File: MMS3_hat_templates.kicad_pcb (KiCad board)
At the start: 4 copper layers, 100 x 50 mm, 55 parts, among them J1 Chainbus in, J2 Chainbus Out, J3 Conn_01x04_Pin, J4 AMASS XT60 Male, J5 AMASS XT60 Female, J8 Conn_01x03_Pin, SW1 SW_DIP_x04, U1 SN74CB3Q3384APW, U2 M24C64, U4 AMS1117, U5 LM2596HVS-ADJRG

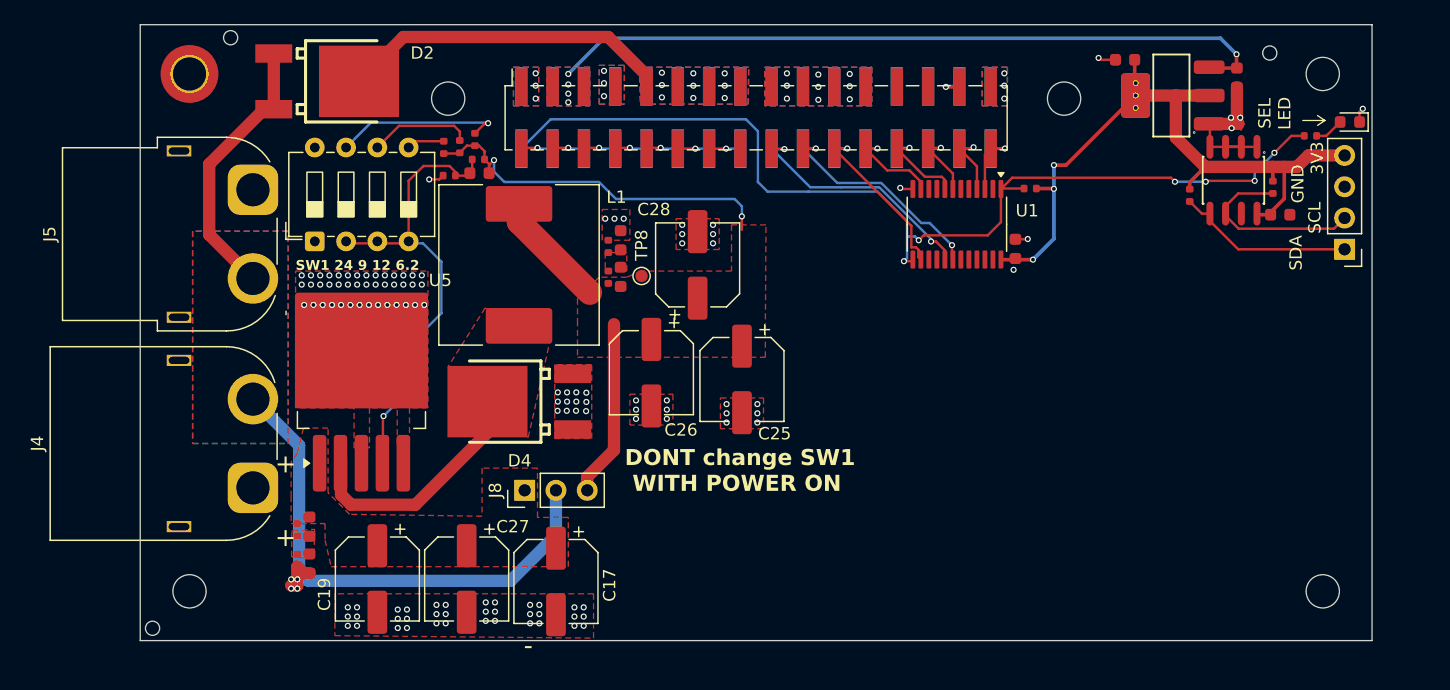
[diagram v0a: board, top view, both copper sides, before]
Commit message: updated Bus switch to one stocked by TME
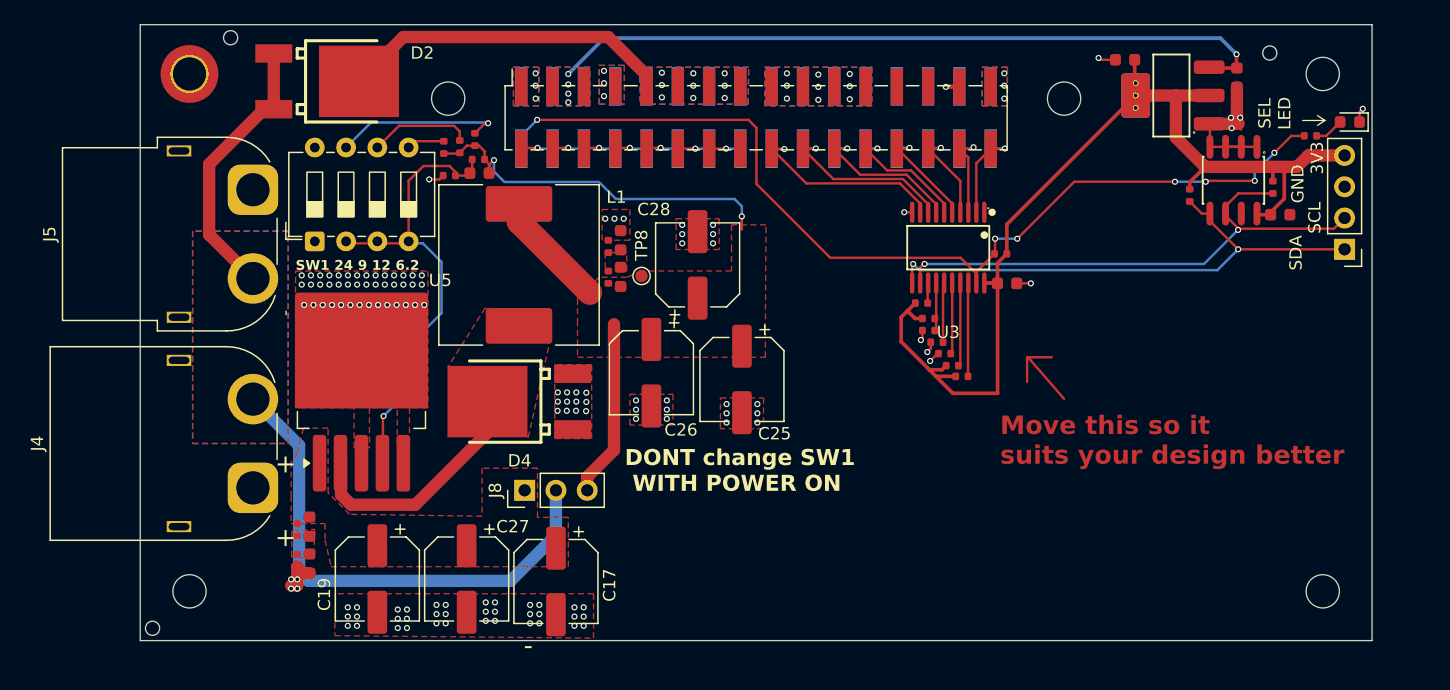
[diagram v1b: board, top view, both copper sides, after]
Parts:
- removed U1: SN74CB3Q3384APW, Package_SO:TSSOP-24_4.4x7.8mm_P0.65mm
- added R19: 10kΩ, PCM_JLCPCB:R_0402, F.Cu at (143.3, 114.7)
- added R20: 10kΩ, PCM_JLCPCB:R_0402, F.Cu at (142.7, 113.8)
- added R5: 10kΩ, PCM_JLCPCB:R_0402, F.Cu at (144.7, 116.5)
- added R6: 10kΩ, PCM_JLCPCB:R_0402, F.Cu at (143.9, 115.7)
- added R7: 10kΩ, PCM_JLCPCB:R_0402, F.Cu at (141.4, 110.6)
- added R8: 10kΩ, PCM_JLCPCB:R_0402, F.Cu at (142.0, 111.8)
- added R9: 10kΩ, PCM_JLCPCB:R_0402, F.Cu at (142.0, 112.8)
- added U3: SN74CB3Q3245PWR, SN74CB3Q3245PWR:TSSOP-20_L6.5-W4.4-P0.65-LS6.4-BL, F.Cu at (143.6, 106.1)
- moved R4 5.82 mm to (147.8, 106.6)
- moved C1 2.88 mm to (148.4, 109.0), turned to 0 degrees
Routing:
- net /Bus_switch/Chainbus.SDA: track 14.5 -> 43.4 mm, vias 0 -> 2
- net /Bus_switch/Chainbus.SCL: track 15.5 -> 43.9 mm, vias 0 -> 2
- net +3V3: track 57.0 -> 83.4 mm, vias 3 -> 0
- net /Bus_switch/Chainbus.RX: track 0.00 -> 7.59 mm
- net /Bus_switch/Chainbus.TX: track 0.00 -> 6.77 mm
- net /Bus_switch/Chainbus.MISO: track 0.00 -> 5.78 mm
- net /Bus_switch/Chainbus.MOSI: track 0.00 -> 4.84 mm
- net /Bus_switch/Chainbus.SCK: track 0.00 -> 3.90 mm
- net /Bus_switch/Chainbus_In.SCL: track 18.6 -> 14.8 mm, vias 2 -> 1
- net /Bus_switch/Chainbus_In.SDA: track 20.4 -> 16.7 mm, vias 2 -> 1
- net /Bus_switch/Chainbus_In.SCK: track 8.13 -> 10.9 mm
- net GND: track 21.6 -> 24.0 mm, vias 142 -> 144
- net /Bus_switch/Chainbus_In.RX: track 5.78 -> 7.96 mm
- net /Bus_switch/Chainbus_In.MISO: track 6.22 -> 8.36 mm
- net /Bus_switch/SEL1: track 82.3 -> 80.3 mm, vias 6 -> 7
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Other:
- board text added: "Move this so it suits your design better"
